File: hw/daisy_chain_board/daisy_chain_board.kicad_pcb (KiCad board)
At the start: 2 copper layers, 65 x 21.2 mm, 9 parts, among them J7 Conn_02x25_Odd_Even, J8 L717SDB25PA4CH4F, X1 Mac, X2 Dogcow, X3 Mac2, X4 Raspberry Pi, X7 Pi

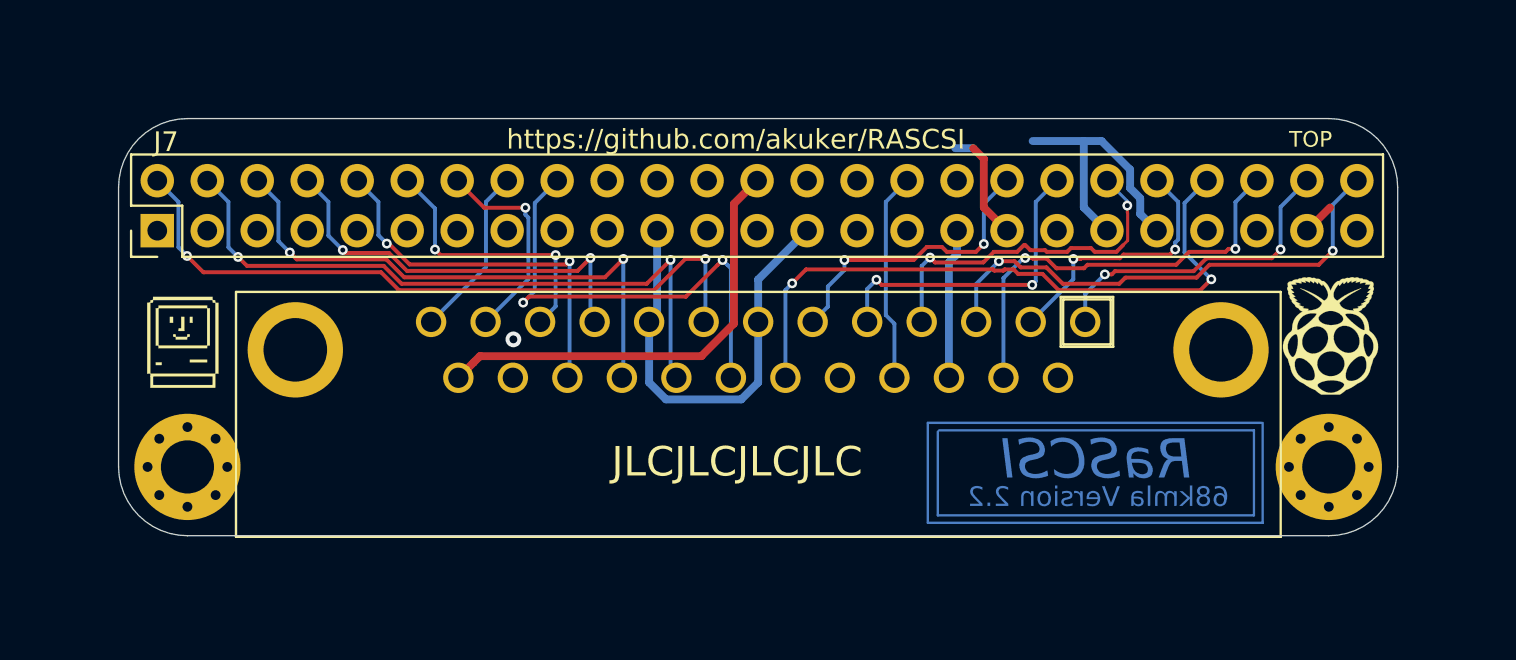
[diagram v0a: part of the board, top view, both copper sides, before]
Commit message: Updated to say RaSCSI Reloaded and silkscreen cleanup
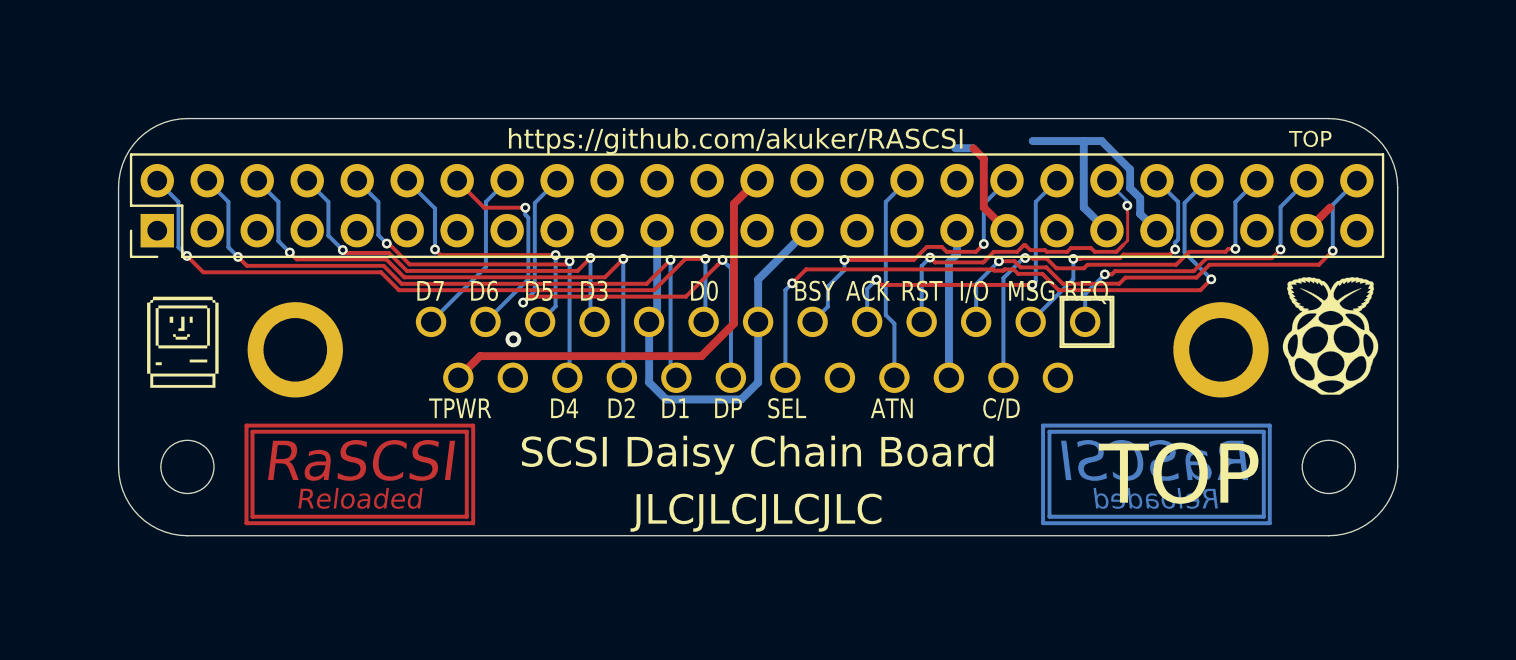
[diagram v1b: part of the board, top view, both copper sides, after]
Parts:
- H5, H6: footprint MountingHole:MountingHole_2.7mm_M2.5_Pad_Via -> MountingHole:MountingHole_2.7mm
- J8: value L717SDB25PA4CH4F -> CONFLY DB25
- moved X2 29.2 mm to (214.6, 94.8)
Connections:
- J7 pad 25: Net-(J7-Pad25) -> unconnected-(J7-Pad25)
- J7 pad 34: Net-(J7-Pad34) -> unconnected-(J7-Pad34)
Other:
- net class Default removed
- board text added: "Reloaded"
- board text removed: "68kmla Version 2.2"

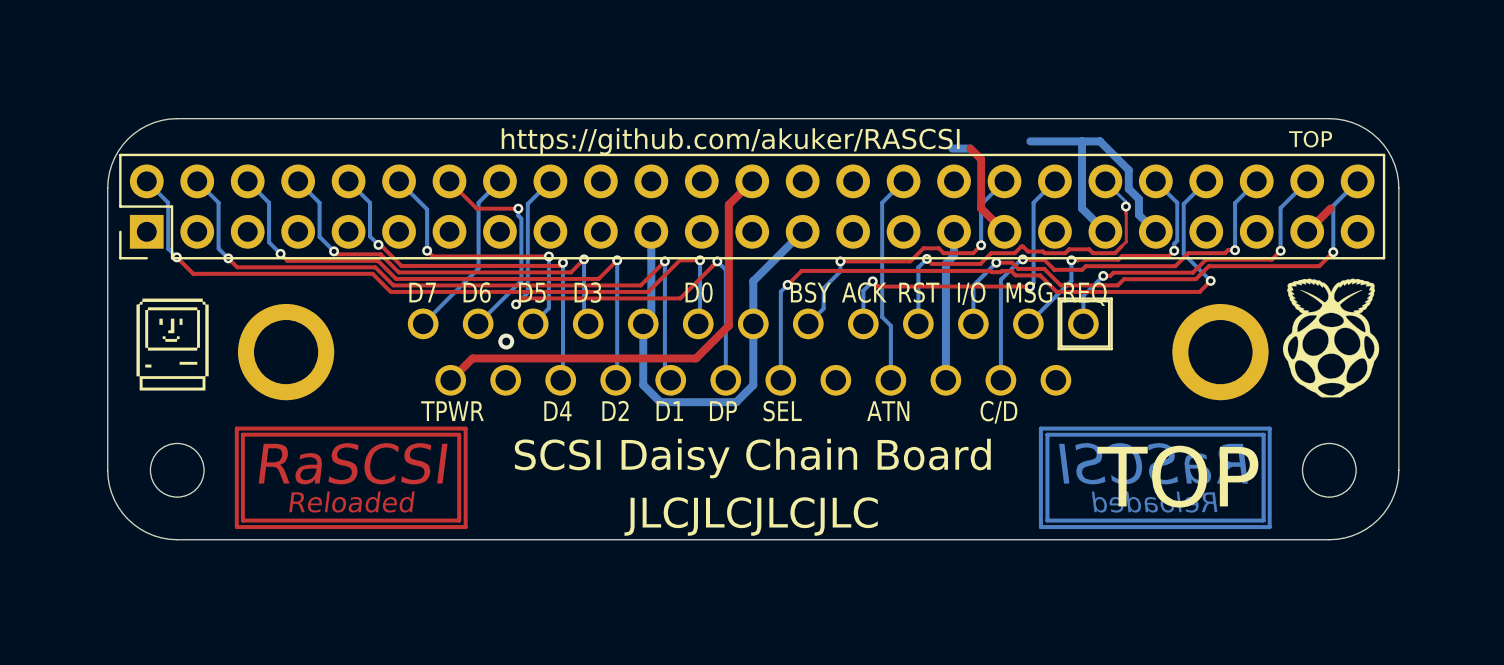
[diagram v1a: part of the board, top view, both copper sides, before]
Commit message: Added pin labels on top side
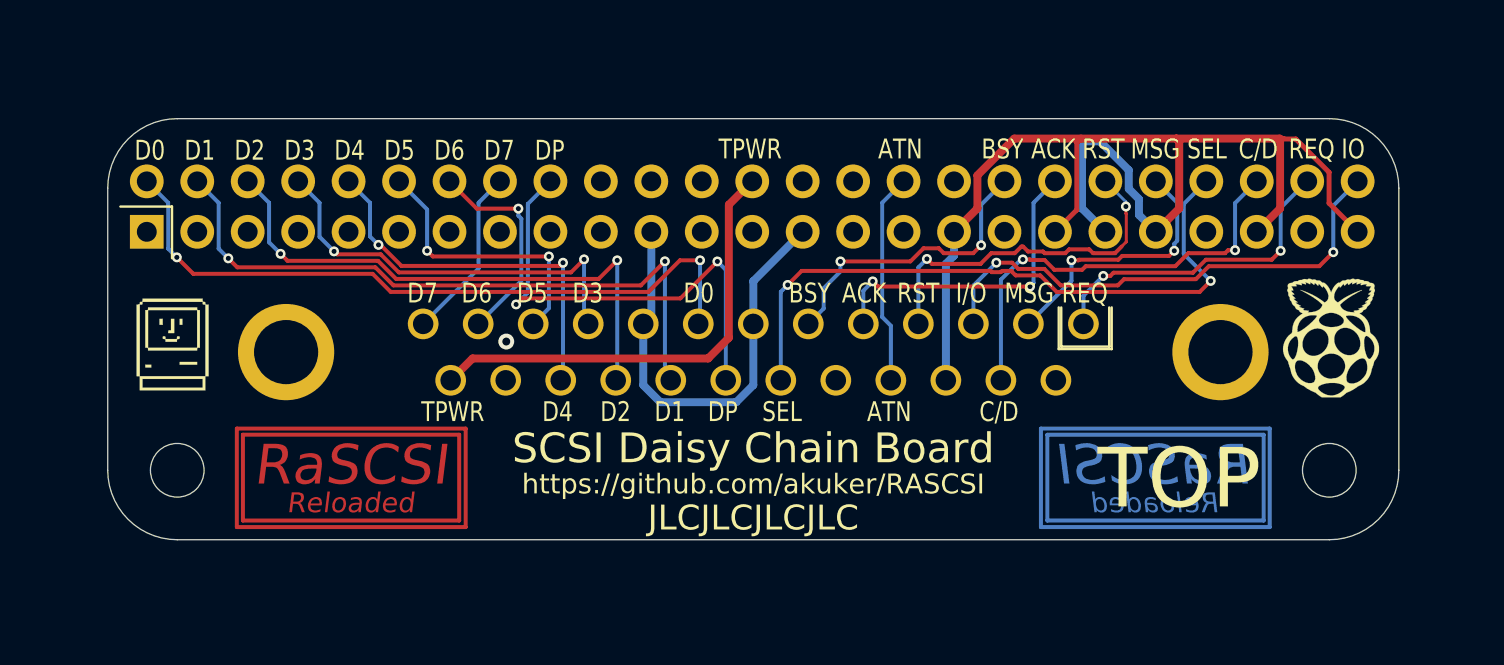
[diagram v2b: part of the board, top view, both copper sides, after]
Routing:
- net GND: track 52.3 -> 84.3 mm
- net C-D5: track 14.6 -> 14.1 mm

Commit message: re-add 3d shapes
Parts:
- removed X2: Dogcow, SamacSys_Parts:dogcow

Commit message: As-ordered version
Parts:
- J7: footprint Connector_PinHeader_2.54mm:PinHeader_2x25_P2.54mm_Vertical -> SamacSys_Parts:Modified_PinHeader_2x25_P2.54mm_Vertical
